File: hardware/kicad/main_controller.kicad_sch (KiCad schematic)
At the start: 38 parts, among them Q1 DMG1012UW, Q2 DMG1012UW, SW1 B3U-3000P, SW2 B3U-3000P, U1 ESP32-C6FH4, Y1 CM315D32768DZFT, Y2 R940000171

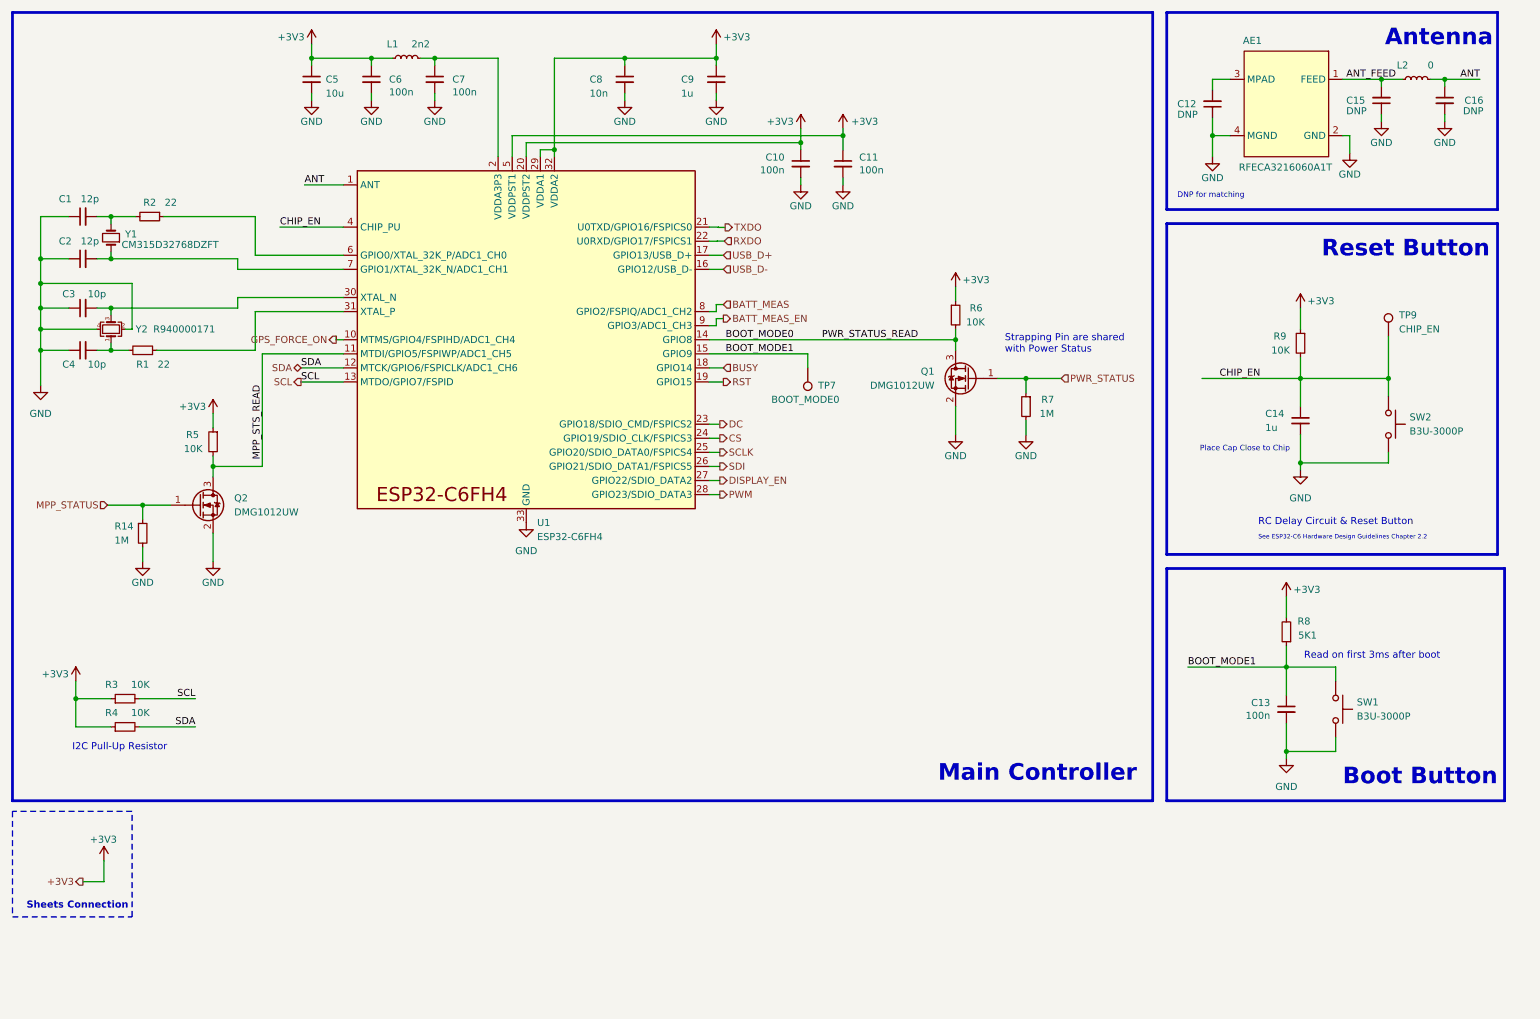
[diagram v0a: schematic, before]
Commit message: update schematics with gnss
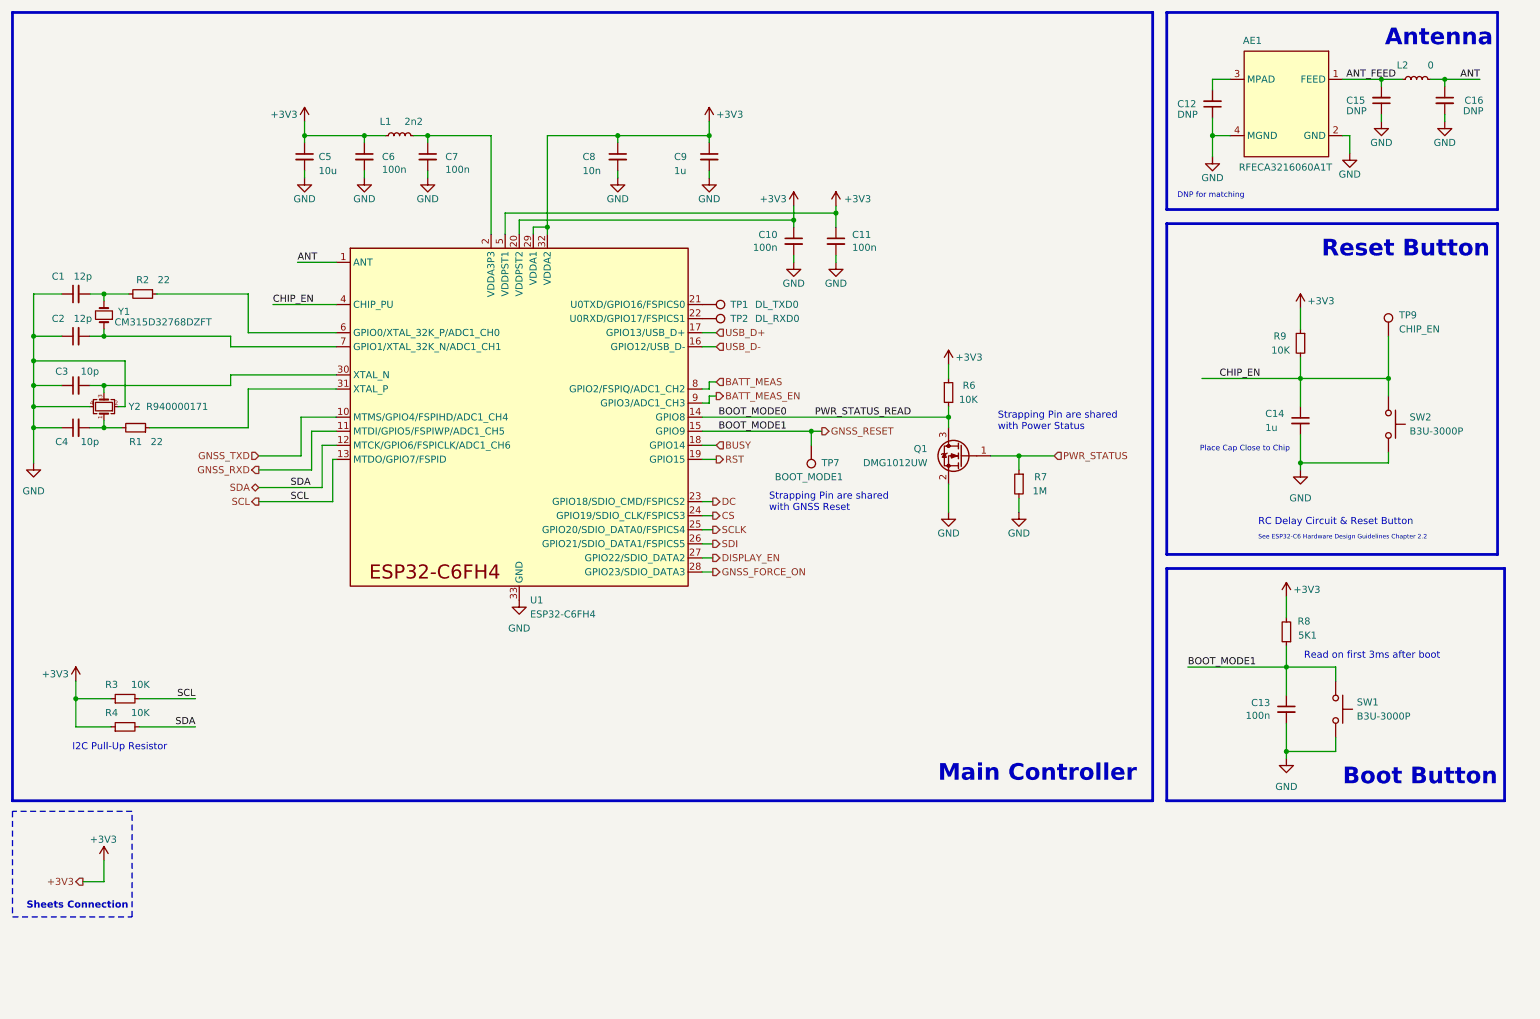
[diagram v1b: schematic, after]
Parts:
- removed Q2: DMG1012UW, Package_TO_SOT_SMD:SOT-323_SC-70, symbol Device:Q_NMOS_GSD
- removed R14: 1M, Resistor_SMD:R_0402_1005Metric, symbol Device:R_Small
- removed R5: 10K, Resistor_SMD:R_0402_1005Metric, symbol Device:R_Small
- added TP1: DL_TXD0, TestPoint:TestPoint_Pad_D1.0mm, symbol Connector:TestPoint
- added TP2: DL_RXD0, TestPoint:TestPoint_Pad_D1.0mm, symbol Connector:TestPoint
- TP7: value BOOT_MODE0 -> BOOT_MODE1
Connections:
- net BOOT_MODE1 renamed GNSS_RESET
- net GPS_FORCE_ON renamed GNSS_TXD
- net MPP_STS_READ renamed GNSS_RXD
- net PWM renamed GNSS_FORCE_ON
- net RXDO: no longer names the net of U1.22 (U0RXD/GPIO17/FSPICS1)
- net RXDO: now also TP2.1
- net TXDO: no longer names the net of U1.21 (U0TXD/GPIO16/FSPICS0)
- net TXDO: now also TP1.1
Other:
- note added: "Strapping Pin are shared with GNSS Reset"
- moved on the sheet: C1, C10, C11, C2, C3, C4, C5, C6, C7, C8, C9, L1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

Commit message: update pcb
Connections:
- net GNSS_RXD: now also U1.10 (MTMS/GPIO4/FSPIHD/ADC1_CH4); no longer U1.11 (MTDI/GPIO5/FSPIWP/ADC1_CH5)
- net GNSS_TXD: now also U1.11 (MTDI/GPIO5/FSPIWP/ADC1_CH5); no longer U1.10 (MTMS/GPIO4/FSPIHD/ADC1_CH4)
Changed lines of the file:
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@@
 	(hierarchical_label "GNSS_RXD"
 		(shape output)
-		(at 58.42 97.79 180)
+		(at 58.42 95.25 180)
 		(fields_autoplaced yes)
 		(effects
@@
 	(hierarchical_label "GNSS_TXD"
 		(shape input)
-		(at 58.42 95.25 180)
+		(at 58.42 97.79 180)
 		(fields_autoplaced yes)
 		(effects

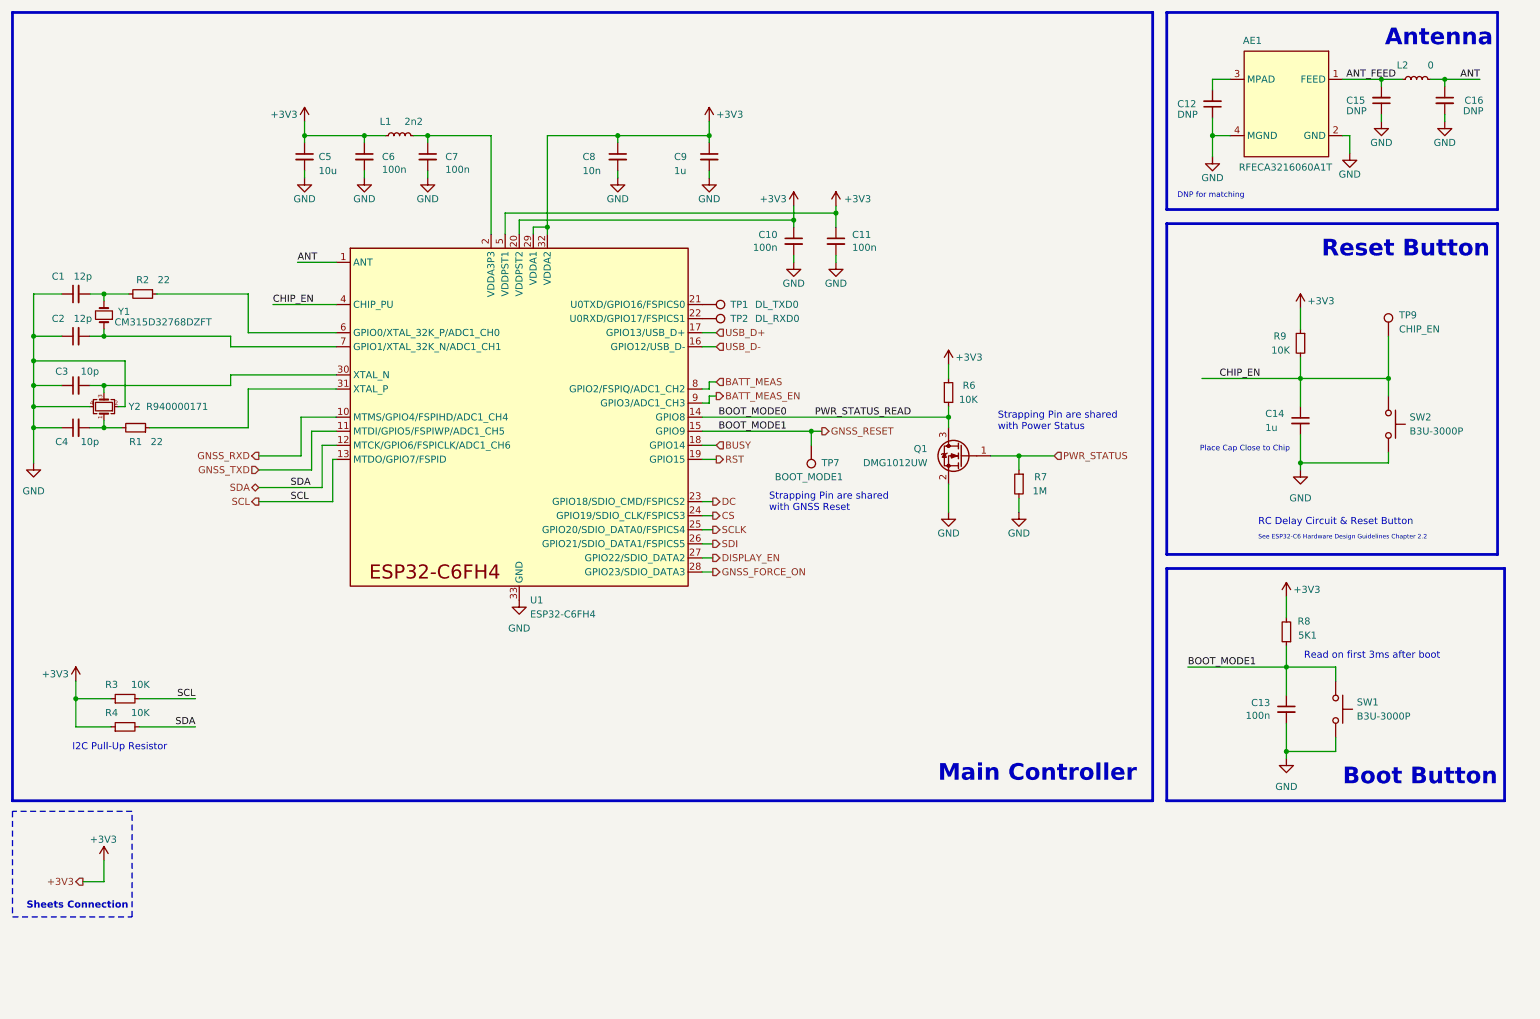
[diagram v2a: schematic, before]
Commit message: add second user button
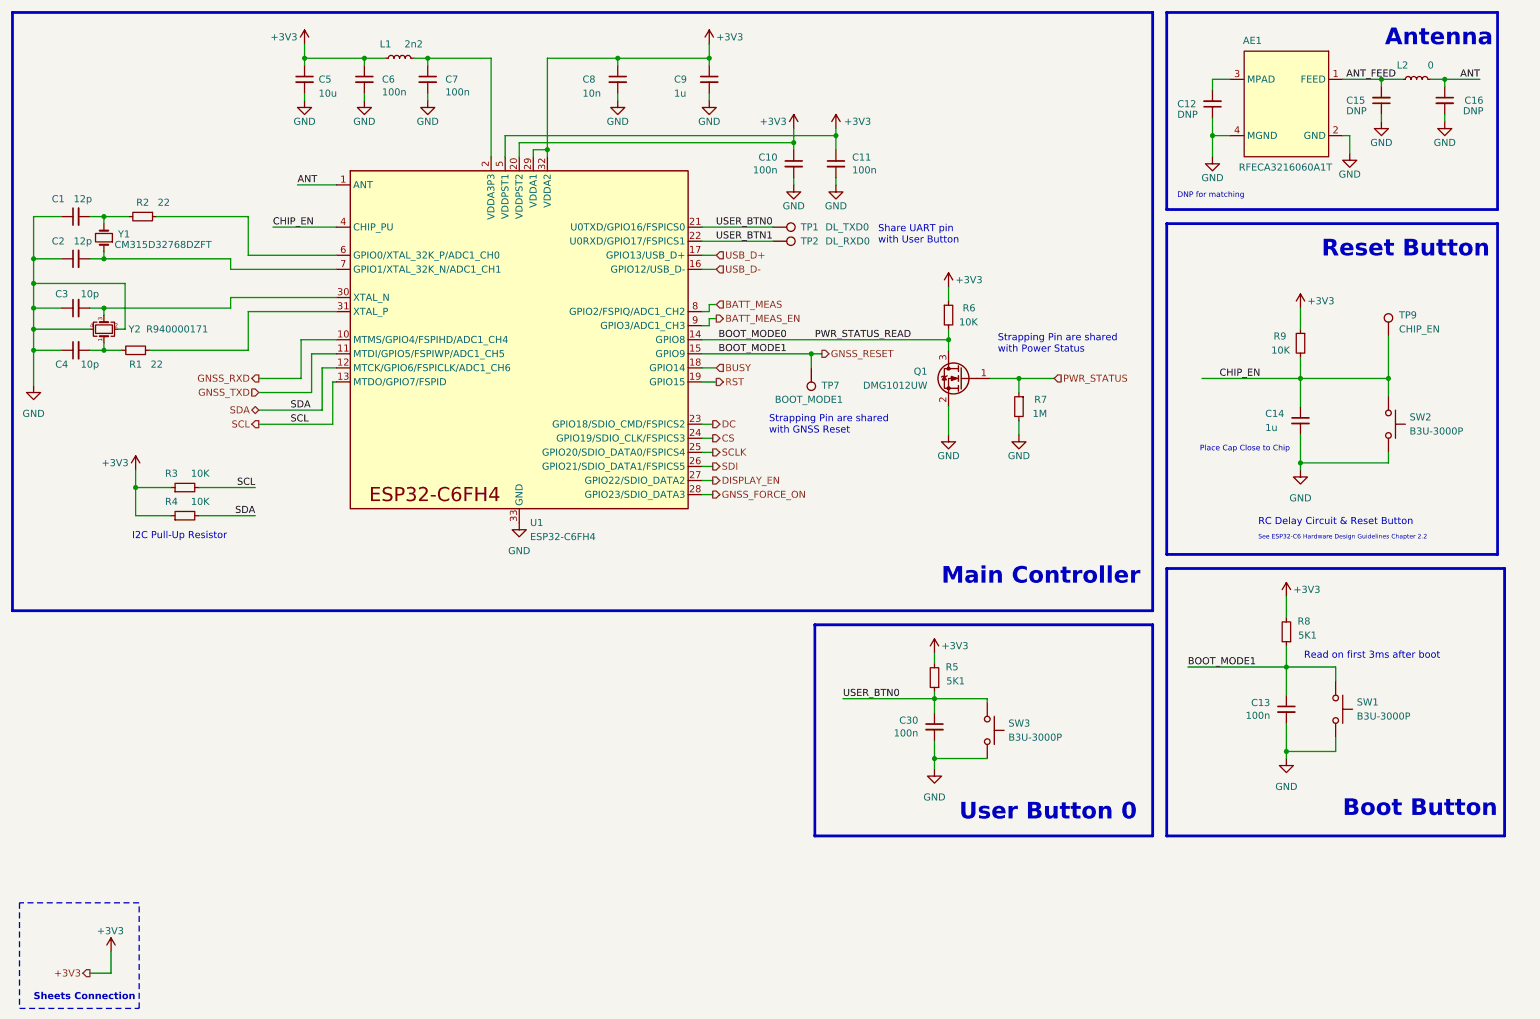
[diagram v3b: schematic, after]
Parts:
- added C30: 100n, Capacitor_SMD:C_0402_1005Metric, symbol Device:C_Small
- added R5: 5K1, Resistor_SMD:R_0402_1005Metric, symbol Device:R_Small
- added SW3: B3U-3000P, atlas:SW_SPST_B3U-3000P, symbol Switch:SW_Push
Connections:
- net +3V3: now also R5.2
- net GND: now also C30.2, SW3.2
- net USER_BTN0: now reaches TP1.1, U1.21 (U0TXD/GPIO16/FSPICS0)
- net USER_BTN0: now also C30.1, R5.1, SW3.1
- net USER_BTN1: now reaches TP2.1, U1.22 (U0RXD/GPIO17/FSPICS1)
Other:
- note added: "Share UART pin with User Button"
- note added: "User Button 0"
- moved on the sheet: C1, C10, C11, C2, C3, C4, C5, C6, C7, C8, C9, L1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
